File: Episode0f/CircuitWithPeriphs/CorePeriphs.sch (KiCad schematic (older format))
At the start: 11 parts, among them J303 Conn_01x05, U301 82C55A, U302 82C54, U303 MC6850

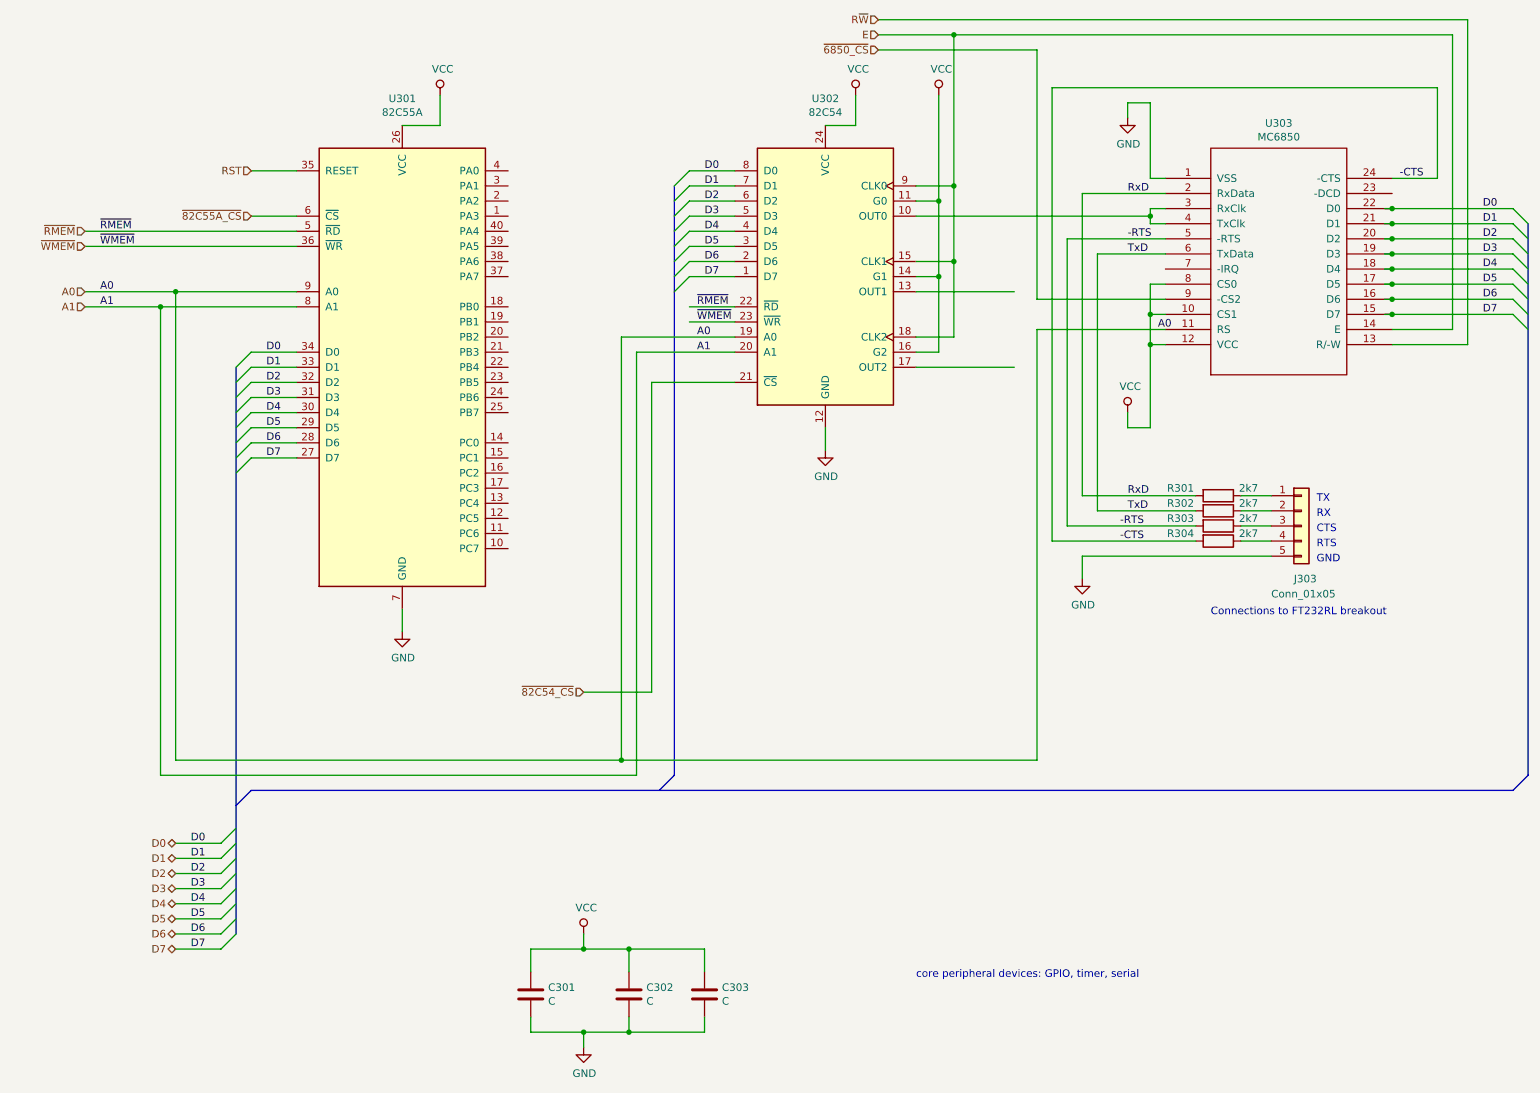
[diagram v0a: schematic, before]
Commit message: correct connections to FT232RL breakout
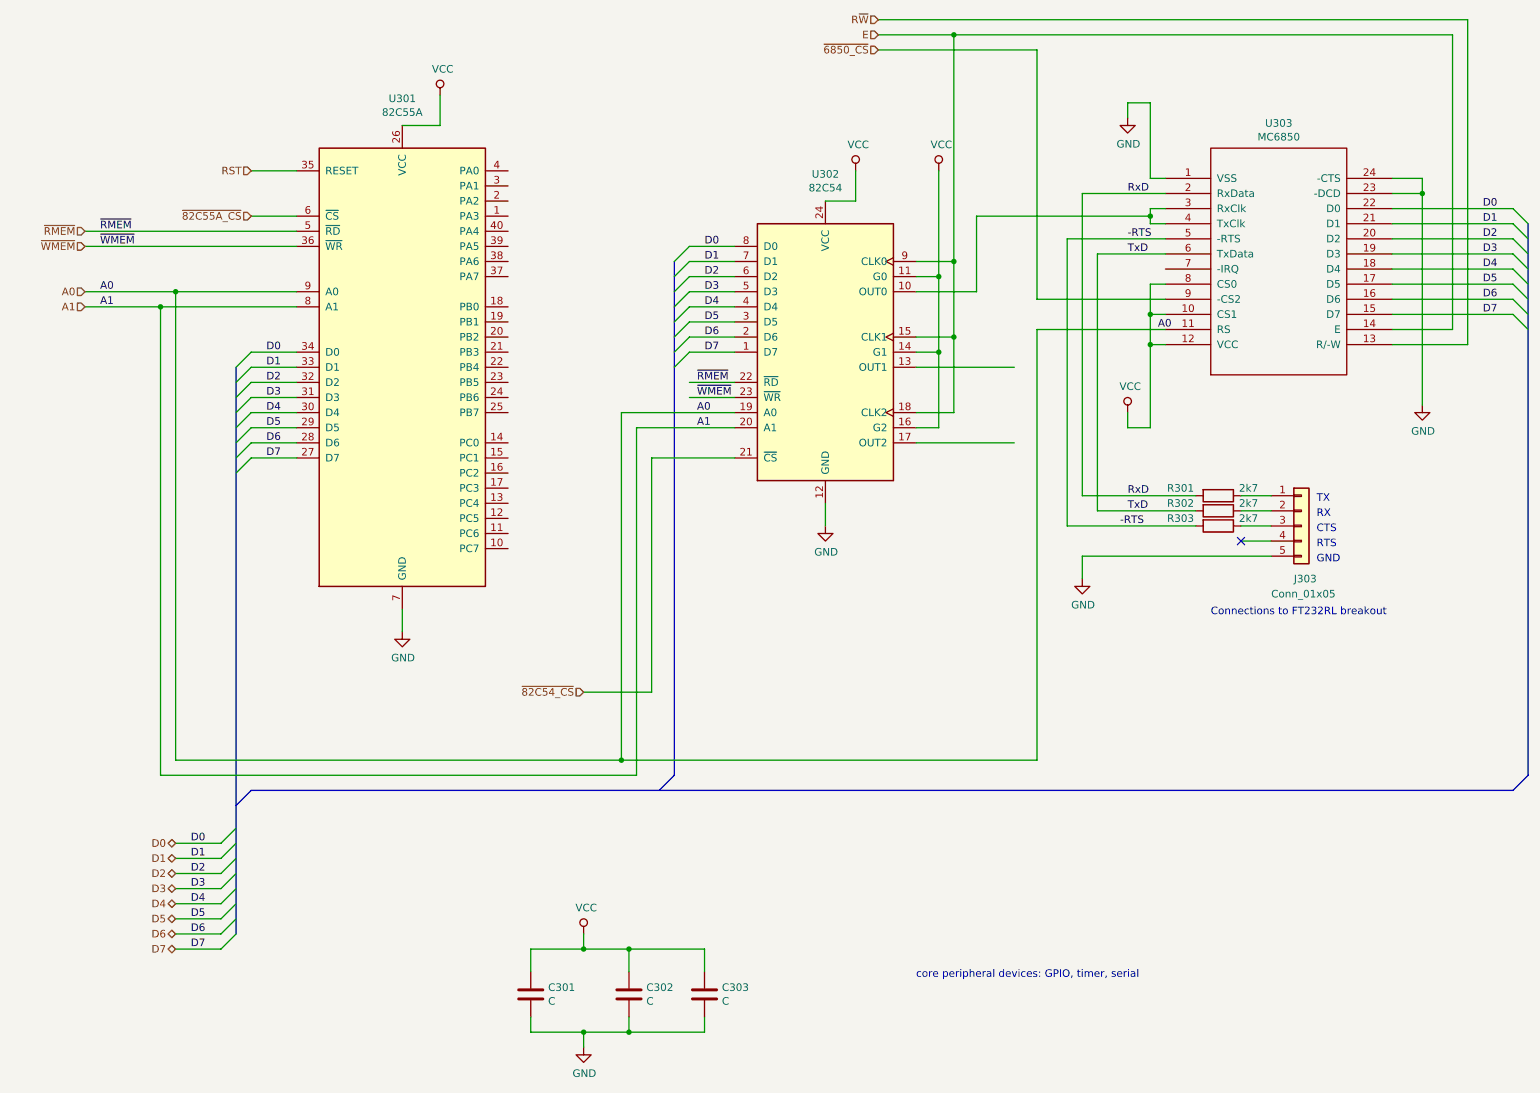
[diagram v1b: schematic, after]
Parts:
- removed R304: 2k7, symbol device:R
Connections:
- net labels removed: -CTS
- wire segments 145 -> 138
- no-connect marks 0 -> 1
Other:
- moved on the sheet: U302
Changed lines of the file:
@@
 L intel:82C54 U302
 U 1 1 5DE12B9A
-P 5750 2300
-F 0 "U302" H 5750 3478 50  0000 C CNN
-F 1 "82C54" H 5750 3387 50  0000 C CNN
-F 2 "Housings_DIP:DIP-24_W15.24mm" H 5800 2550 50  0001 C CNN
-F 3 "http://download.intel.com/design/archives/periphrl/docs/23124406.pdf" H 5300 3200 50  0001 C CNN
-	1    5750 2300
+P 5750 2800
+F 0 "U302" H 5750 3978 50  0000 C CNN
+F 1 "82C54" H 5750 3887 50  0000 C CNN
+F 2 "Housings_DIP:DIP-24_W15.24mm" H 5800 3050 50  0001 C CNN
+F 3 "http://download.intel.com/design/archives/periphrl/docs/23124406.pdf" H 5300 3700 50  0001 C CNN
+	1    5750 2800
 	1    0    0    -1
 $EndComp
@@
 	1750 6750 1850 6650
 Wire Wire Line
-	5150 1600 4850 1600
-Wire Wire Line
-	5150 1700 4850 1700
-Wire Wire Line
-	5150 1800 4850 1800
-Wire Wire Line
-	5150 1900 4850 1900
-Wire Wire Line
-	5150 2000 4850 2000
-Wire Wire Line
 	5150 2100 4850 2100
 Wire Wire Line
@@
 Wire Wire Line
 	5150 2300 4850 2300
-Text Label 4950 1600 0    50   ~ 0
+Wire Wire Line
+	5150 2400 4850 2400
+Wire Wire Line
+	5150 2500 4850 2500
+Wire Wire Line
+	5150 2600 4850 2600
+Wire Wire Line
+	5150 2700 4850 2700
+Wire Wire Line
+	5150 2800 4850 2800
+Text Label 4950 2100 0    50   ~ 0
 D0
-Text Label 4950 1700 0    50   ~ 0
+Text Label 4950 2200 0    50   ~ 0
 D1
-Text Label 4950 1800 0    50   ~ 0
+Text Label 4950 2300 0    50   ~ 0
 D2
-Text Label 4950 1900 0    50   ~ 0
+Text Label 4950 2400 0    50   ~ 0
 D3
-Text Label 4950 2000 0    50   ~ 0
+Text Label 4950 2500 0    50   ~ 0
 D4
-Text Label 4950 2100 0    50   ~ 0
+Text Label 4950 2600 0    50   ~ 0
 D5
-Text Label 4950 2200 0    50   ~ 0
+Text Label 4950 2700 0    50   ~ 0
 D6
-Text Label 4950 2300 0    50   ~ 0
+Text Label 4950 2800 0    50   ~ 0
 D7
 Entry Wire Line
-	4750 1700 4850 1600
-Entry Wire Line
-	4750 1800 4850 1700
-Entry Wire Line
-	4750 1900 4850 1800
-Entry Wire Line
-	4750 2000 4850 1900
-Entry Wire Line
-	4750 2100 4850 2000
-Entry Wire Line
 	4750 2200 4850 2100
 Entry Wire Line
@@
 Entry Wire Line
 	4750 2400 4850 2300
+Entry Wire Line
+	4750 2500 4850 2400
+Entry Wire Line
+	4750 2600 4850 2500
+Entry Wire Line
+	4750 2700 4850 2600
+Entry Wire Line
+	4750 2800 4850 2700
+Entry Wire Line
+	4750 2900 4850 2800
 Text Label 950  2000 0    50   ~ 0
 ~RMEM
@@
 	4650 5700 4750 5600
 Wire Wire Line
-	5150 2500 4850 2500
-Wire Wire Line
-	5150 2600 4850 2600
-Text Label 4900 2500 0    50   ~ 0
+	5150 3000 4850 3000
+Wire Wire Line
+	5150 3100 4850 3100
+Text Label 4900 3000 0    50   ~ 0
 ~RMEM
-Text Label 4900 2600 0    50   ~ 0
+Text Label 4900 3100 0    50   ~ 0
 ~WMEM
 Text Label 950  2400 0    50   ~ 0
@@
 Text Label 950  2500 0    50   ~ 0
 A1
-Text Label 4900 2700 0    50   ~ 0
+Text Label 4900 3200 0    50   ~ 0
 A0
-Text Label 4900 2800 0    50   ~ 0
+Text Label 4900 3300 0    50   ~ 0
 A1
 Wire Wire Line
-	5750 1300 5950 1300
-Wire Wire Line
-	5950 1300 5950 1100
+	5750 1800 5950 1800
+Wire Wire Line
+	5950 1800 5950 1600
 $Comp
 L power:VCC #PWR?
 U 1 1 5DE1D53F
-P 5950 1100
-F 0 "#PWR?" H 5950 950 50  0001 C CNN
-F 1 "VCC" H 5967 1273 50  0000 C CNN
-F 2 "" H 5950 1100 50  0001 C CNN
-F 3 "" H 5950 1100 50  0001 C CNN
-	1    5950 1100
+P 5950 1600
+F 0 "#PWR?" H 5950 1450 50  0001 C CNN
+F 1 "VCC" H 5967 1773 50  0000 C CNN
+F 2 "" H 5950 1600 50  0001 C CNN
+F 3 "" H 5950 1600 50  0001 C CNN
+	1    5950 1600
 	1    0    0    -1
 $EndComp
@@
 ~82C54_CS
 Wire Wire Line
-	5150 3000 4600 3000
-Wire Wire Line
-	4600 3000 4600 5050
+	5150 3500 4600 3500
+Wire Wire Line
+	4600 3500 4600 5050
 Wire Wire Line
 	4600 5050 4150 5050
 Wire Wire Line
-	5750 3300 5750 3450
+	5750 3800 5750 3950
 $Comp
 L power:GND #PWR?
 U 1 1 5DE1F2AE
-P 5750 3450
-F 0 "#PWR?" H 5750 3200 50  0001 C CNN
-F 1 "GND" H 5755 3277 50  0000 C CNN
-F 2 "" H 5750 3450 50  0001 C CNN
-F 3 "" H 5750 3450 50  0001 C CNN
-	1    5750 3450
+P 5750 3950
+F 0 "#PWR?" H 5750 3700 50  0001 C CNN
+F 1 "GND" H 5755 3777 50  0000 C CNN
+F 2 "" H 5750 3950 50  0001 C CNN
+F 3 "" H 5750 3950 50  0001 C CNN
+	1    5750 3950
 	1    0    0    -1
 $EndComp
@@
 Connection ~ 4150 7300
 Wire Wire Line
-	6350 2800 6500 2800
-Wire Wire Line
-	6500 2800 6500 2300
+	6350 3300 6500 3300
+Wire Wire Line
+	6500 3300 6500 2800
 $Comp
 L power:VCC #PWR?
 U 1 1 5DE3C94B
-P 6500 1100
-F 0 "#PWR?" H 6500 950 50  0001 C CNN
-F 1 "VCC" H 6517 1273 50  0000 C CNN
-F 2 "" H 6500 1100 50  0001 C CNN
-F 3 "" H 6500 1100 50  0001 C CNN
-	1    6500 1100
-	1    0    0    -1
-$EndComp
-Wire Wire Line
-	6350 1800 6500 1800
-Connection ~ 6500 1800
-Wire Wire Line
-	6500 1800 6500 1100
+P 6500 1600
+F 0 "#PWR?" H 6500 1450 50  0001 C CNN
+F 1 "VCC" H 6517 1773 50  0000 C CNN
+F 2 "" H 6500 1600 50  0001 C CNN
+F 3 "" H 6500 1600 50  0001 C CNN
+	1    6500 1600
+	1    0    0    -1
+$EndComp
 Wire Wire Line
 	6350 2300 6500 2300
 Connection ~ 6500 2300
 Wire Wire Line
-	6500 2300 6500 1800
+	6500 2300 6500 1600
+Wire Wire Line
+	6350 2800 6500 2800
+Connection ~ 6500 2800
+Wire Wire Line
+	6500 2800 6500 2300
 Text HLabel 6100 700  0    50   Input ~ 0
 E
 Wire Wire Line
-	6350 2700 6600 2700
-Wire Wire Line
-	6600 2700 6600 2200
+	6350 3200 6600 3200
+Wire Wire Line
+	6600 3200 6600 2700
 Wire Wire Line
 	6600 700  6100 700
-Wire Wire Line
-	6350 1700 6600 1700
-Connection ~ 6600 1700
-Wire Wire Line
-	6600 1700 6600 700
 Wire Wire Line
 	6350 2200 6600 2200
 Connection ~ 6600 2200
 Wire Wire Line
-	6600 2200 6600 1700
-Wire Wire Line
-	6350 2400 7000 2400
+	6600 2200 6600 700
+Wire Wire Line
+	6350 2700 6600 2700
+Connection ~ 6600 2700
+Wire Wire Line
+	6600 2700 6600 2200
 Wire Wire Line
 	6350 2900 7000 2900
+Wire Wire Line
+	6350 3400 7000 3400
 $Comp
 L MC6850:MC6850 U303
@@
 	1    0    0    -1
 $EndComp
-Wire Wire Line
-	9450 1850 9500 1850
-Wire Wire Line
-	9450 1950 9500 1950
-Wire Wire Line
-	9450 2050 9500 2050
-Wire Wire Line
-	9450 2150 9500 2150
-Wire Wire Line
-	9450 2250 9500 2250
-Wire Wire Line
-	9450 2350 9500 2350
-Wire Wire Line
-	9450 2450 9500 2450
-Wire Wire Line
-	9450 2550 9500 2550
 Text Label 10100 1850 0    50   ~ 0
 D0
@@
 	10000 600  6100 600
 Wire Wire Line
-	7900 1900 7900 1850
-Wire Wire Line
 	7900 1850 8000 1850
 Wire Wire Line
-	6350 1900 7900 1900
-Wire Wire Line
 	8000 1950 7900 1950
-Wire Wire Line
-	7900 1950 7900 1900
-Connection ~ 7900 1900
 Text HLabel 6100 800  0    50   Input ~ 0
 ~6850_CS
@@
 	7350 2050 7350 3950
 Wire Wire Line
-	9500 1650 9800 1650
-Wire Wire Line
-	9800 1650 9800 1050
-Wire Wire Line
-	9800 1050 7250 1050
-Wire Wire Line
-	7250 1050 7250 4050
+	9500 1650 9700 1650
 Wire Wire Line
 	7450 4150 7450 4300
@@
 	0    1    1    0
 $EndComp
-$Comp
-L device:R R304
-U 1 1 5DE98EA2
-P 8350 4050
-F 0 "R304" V 8300 3800 50  0000 C CNN
-F 1 "2k7" V 8300 4250 50  0000 C CNN
-F 2 "" V 8280 4050 50  0001 C CNN
-F 3 "" H 8350 4050 50  0001 C CNN
-	1    8350 4050
-	0    1    1    0
-$EndComp
 Wire Wire Line
 	7450 3750 8200 3750
@@
 	7350 3950 8200 3950
 Wire Wire Line
-	7250 4050 8200 4050
-Wire Wire Line
 	8500 3750 8700 3750
 Wire Wire Line
@@
 Wire Wire Line
 	8500 3950 8700 3950
-Wire Wire Line
-	8500 4050 8700 4050
 Text Label 7950 2650 0    50   ~ 0
 A0
 Wire Wire Line
-	4400 2700 4400 5500
+	4400 3200 4400 5500
 Wire Wire Line
 	4400 5500 1450 5500
@@
 	1450 5500 1450 2400
 Wire Wire Line
-	4400 2700 5150 2700
+	4400 3200 5150 3200
 Connection ~ 1450 2400
 Wire Wire Line
 	1450 2400 850  2400
 Wire Wire Line
-	4500 2800 4500 5600
+	4500 3300 4500 5600
 Wire Wire Line
 	4500 5600 1350 5600
@@
 	1350 5600 1350 2500
 Wire Wire Line
-	4500 2800 5150 2800
+	4500 3300 5150 3300
 Connection ~ 1350 2500
 Wire Wire Line
@@
 	7150 2650 8000 2650
 Connection ~ 4400 5500
-Text Label 9550 1650 0    50   ~ 0
--CTS
-Text Label 7700 4050 0    50   ~ 0
--CTS
 Text Label 7700 3950 0    50   ~ 0
 -RTS
@@
 Text Label 7750 3750 0    50   ~ 0
 RxD
-Connection ~ 9500 1850
 Wire Wire Line
 	9500 1850 10300 1850
-Connection ~ 9500 1950
 Wire Wire Line
 	9500 1950 10300 1950
-Connection ~ 9500 2050
 Wire Wire Line
 	9500 2050 10300 2050
-Connection ~ 9500 2150
 Wire Wire Line
 	9500 2150 10300 2150
-Connection ~ 9500 2250
 Wire Wire Line
 	9500 2250 10300 2250
-Connection ~ 9500 2350
 Wire Wire Line
 	9500 2350 10300 2350
-Connection ~ 9500 2450
 Wire Wire Line
 	9500 2450 10300 2450
-Connection ~ 9500 2550
 Wire Wire Line
 	9500 2550 10300 2550
+Wire Wire Line
+	9700 1650 9700 1750
+$Comp
+L power:GND #PWR?
+U 1 1 5E14BF6A
+P 9700 3150
+F 0 "#PWR?" H 9700 2900 50  0001 C CNN
+F 1 "GND" H 9705 2977 50  0000 C CNN
+F 2 "" H 9700 3150 50  0001 C CNN
+F 3 "" H 9700 3150 50  0001 C CNN
+	1    9700 3150
+	1    0    0    -1
+$EndComp
+Wire Wire Line
+	9500 1750 9700 1750
+Connection ~ 9700 1750
+Wire Wire Line
+	9700 1750 9700 3150
+Wire Wire Line
+	8700 4050 8500 4050
+NoConn ~ 8500 4050
+Wire Wire Line
+	7900 1850 7900 1900
+Wire Wire Line
+	6350 2400 6750 2400
+Wire Wire Line
+	6750 2400 6750 1900
+Wire Wire Line
+	6750 1900 7900 1900
+Connection ~ 7900 1900
+Wire Wire Line
+	7900 1900 7900 1950
 Wire Bus Line
 	1950 5700 10300 5700
 Wire Bus Line
-	4750 1700 4750 5600
+	4750 2200 4750 5600
 Wire Bus Line
 	10400 1950 10400 5600
